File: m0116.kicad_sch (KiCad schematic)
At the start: 247 parts, among them J2 Conn_01x04_MountingPin, J3 Conn_01x04_MountingPin, Q1 Q_PMOS_GSD AO3401A, Q2 Q_NMOS_GSD 2N7002, Q3 Q_NMOS_GSD 2N7002, Q4 2N3904, SW1 SW_Push, U1 XC6206P332MR, U2 74AHCT1G125, U3 STM32F411RETx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

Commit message: updates
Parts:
- removed SW_RGUI_3: mx-alps-nec, Alps_Only:ALPS-1U, symbol MX_Alps_Hybrid:mx-alps-nec
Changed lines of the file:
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@@
     (stroke (width 0) (type default))
   )
-  (wire (pts (xy 186.69 344.17) (xy 186.69 345.44))
-    (stroke (width 0) (type default))
-  )
   (wire (pts (xy 193.04 309.88) (xy 195.58 309.88))
     (stroke (width 0) (type solid))
@@
         )
       )
-    )
-  )
-  (symbol (lib_id "MX_Alps_Hybrid:mx-alps-nec") (at 182.88 346.71 0) (unit 1)
-    (in_bom yes) (on_board yes) (dnp no)
-    (property "Reference" "SW_RGUI_3" (at 183.7182 341.0458 0)
-      (effects (font (size 1.524 1.524)))
-    )
-    (property "Value" "mx-alps-nec" (at 183.7182 342.9254 0)
-      (effects (font (size 0.508 0.508)))
-    )
-    (property "Footprint" "Alps_Only:ALPS-1U" (at 167.005 347.345 0)
-      (effects (font (size 1.524 1.524)) hide)
-    )
-    (property "Datasheet" "" (at 167.005 347.345 0)
-      (effects (font (size 1.524 1.524)) hide)
-    )
-    (pin "1")
-    (pin "2")
-    (instances
-      (project "m0116"
-        (path "/151da08b-0979-4785-a9bf-6fa9b165d629"
-          (reference "SW_RGUI_3") (unit 1)
-        )
-      )

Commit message: fixes
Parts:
- added SW_RALT_4, SW_SP2_4: mx-alps-nec, Alps_Only:ALPS-1U, symbol MX_Alps_Hybrid:mx-alps-nec
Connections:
- net COL6: now also SW_SP2_4.1 (COL)
- net COL8: now also SW_RALT_4.1 (COL)
- net at D7.2 (A), SW_RALT_1.2 (ROW), SW_RALT_2.2 (ROW)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: now also SW_RALT_4.2 (ROW)
- net at D99.2 (A), SW_SP2_1.2 (ROW), SW_SP2_2.2 (ROW)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: now also SW_SP2_4.2 (ROW)
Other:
- note added: "1.25"
- note added: "1.5u"
- note added: "6.25u at101w"
- note added: "6.5u aek"
- note added: "aek"
- note added: "caps 1 is m0116 caps"
- note added: "caps 2 is iso extra rshift for m0118"
- note added: "grid"
- note added: "m0116 with splits"
- note added: "m0118"
- note added: "m0118 iso rsh extra"
- moved on the sheet: D100, D101, D102, D103, D104, D105, D106, D107, D108, D2, D6, D7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

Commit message: fixes
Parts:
- added SW_BACKSL_2: mx-alps-nec, Alps_Only:ALPS-1U, symbol MX_Alps_Hybrid:mx-alps-nec
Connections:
- net COL13: now also SW_BACKSL_2.1 (COL)
- net at D12.2 (A), SW_BACKSL_1.2 (ROW): now also SW_BACKSL_2.2 (ROW)
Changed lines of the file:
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@@
   (junction (at 250.19 285.75) (diameter 0) (color 0 0 0 0)
   )
+  (junction (at 243.84 290.83) (diameter 0) (color 0 0 0 0)
+  )
   (junction (at 233.68 323.85) (diameter 0) (color 0 0 0 0)
   )
@@
     (stroke (width 0) (type default))
   )
+  (wire (pts (xy 243.84 292.1) (xy 243.84 290.83))
+    (stroke (width 0) (type default))
+  )
   (wire (pts (xy 91.44 21.59) (xy 97.79 21.59))
     (stroke (width 0) (type default))
@@
     (stroke (width 0) (type default))
   )
+  (wire (pts (xy 243.84 290.83) (xy 245.11 290.83))
+    (stroke (width 0) (type solid))
+  )
   (wire (pts (xy 233.68 285.75) (xy 233.68 304.8))
     (stroke (width 0) (type solid))
@@
     (stroke (width 0) (type solid))
   )
+  (wire (pts (xy 250.19 285.75) (xy 251.46 285.75))
+    (stroke (width 0) (type default))
+  )
   (wire (pts (xy 36.83 38.1) (xy 36.83 35.56))
     (stroke (width 0) (type default))
@@
     (stroke (width 0) (type default))
   )
+  (wire (pts (xy 251.46 285.75) (xy 251.46 287.02))
+    (stroke (width 0) (type default))
+  )
   (wire (pts (xy 209.55 290.83) (xy 212.09 290.83))
     (stroke (width 0) (type solid))
@@
     (stroke (width 0) (type default))
   )
-  (wire (pts (xy 242.57 290.83) (xy 245.11 290.83))
+  (wire (pts (xy 242.57 290.83) (xy 243.84 290.83))
     (stroke (width 0) (type solid))
   )
@@
     (stroke (width 0) (type solid))
   )
+  (wire (pts (xy 246.38 292.1) (xy 243.84 292.1))
+    (stroke (width 0) (type default))
+  )
   (wire (pts (xy 162.56 361.95) (xy 160.02 361.95))
     (stroke (width 0) (type default))
@@
         )
       )
+    )
+  )
+  (symbol (lib_id "MX_Alps_Hybrid:mx-alps-nec") (at 247.65 288.29 0) (unit 1)
+    (in_bom yes) (on_board yes) (dnp no)
+    (property "Reference" "SW_BACKSL_2" (at 248.4882 282.6258 0)
+      (effects (font (size 1.524 1.524)))
+    )
+    (property "Value" "mx-alps-nec" (at 248.4882 284.5054 0)
+      (effects (font (size 0.508 0.508)))
+    )
+    (property "Footprint" "Alps_Only:ALPS-1U" (at 231.775 288.925 0)
+      (effects (font (size 1.524 1.524)) hide)
+    )
+    (property "Datasheet" "" (at 231.775 288.925 0)
+      (effects (font (size 1.524 1.524)) hide)
+    )
+    (pin "1")
+    (pin "2")
+    (instances
+      (project "m0116"
+        (path "/151da08b-0979-4785-a9bf-6fa9b165d629"
+          (reference "SW_BACKSL_2") (unit 1)
+        )
+      )

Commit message: update
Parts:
- added SW_LALT_4, SW_SP2_5: mx-alps-nec, Alps_Only:ALPS-1U, symbol MX_Alps_Hybrid:mx-alps-nec
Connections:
- net COL3: now also SW_LALT_4.1 (COL)
- net COL6: now also SW_SP2_5.1 (COL)
- net at D99.2 (A), SW_SP2_1.2 (ROW), SW_SP2_2.2 (ROW)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: now also SW_SP2_5.2 (ROW)
- net at D98.2 (A), SW_LALT_1.2 (ROW), SW_LALT_2.2 (ROW)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: now also SW_LALT_4.2 (ROW)
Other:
- note added: "1.5 post-2.5"
- note added: "6.5 post 4"
- moved on the sheet: D98, D99

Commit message: update
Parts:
- added SW_RCTRL_3, SW_RGUI_3: mx-alps-nec, Alps_Only:ALPS-1U, symbol MX_Alps_Hybrid:mx-alps-nec
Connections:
- net COL10: now also SW_RCTRL_3.1 (COL)
- net COL9: now also SW_RGUI_3.1 (COL)
- net at D100.2 (A), SW_RGUI_1.2 (ROW), SW_RGUI_2.2 (ROW): now also SW_RGUI_3.2 (ROW)
- net at D8.2 (A), SW_RCTRL_1.2 (ROW), SW_RCTRL_2.2 (ROW): now also SW_RCTRL_3.2 (ROW)
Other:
- note added: "1.5"
- note added: "1u"
- moved on the sheet: SW_RALT_4
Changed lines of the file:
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@@
   (junction (at 160.02 361.95) (diameter 0) (color 0 0 0 0)
   )
+  (junction (at 160.02 377.19) (diameter 0) (color 0 0 0 0)
+  )
   (junction (at 204.47 65.405) (diameter 0) (color 0 0 0 0)
   )
@@
   (junction (at 196.85 36.83) (diameter 0) (color 0 0 0 0)
   )
+  (junction (at 193.04 377.19) (diameter 0) (color 0 0 0 0)
+  )
   (junction (at 257.81 295.91) (diameter 0) (color 0 0 0 0)
   )
@@
   (junction (at 217.17 285.75) (diameter 1.016) (color 0 0 0 0)
   )
-  (junction (at 160.02 378.46) (diameter 0) (color 0 0 0 0)
-  )
   (junction (at 220.98 29.21) (diameter 0) (color 0 0 0 0)
   )
@@
   (junction (at 233.68 266.7) (diameter 1.016) (color 0 0 0 0)
   )
+  (junction (at 200.66 356.87) (diameter 0) (color 0 0 0 0)
+  )
   (junction (at 298.45 285.75) (diameter 1.016) (color 0 0 0 0)
   )
@@
   (junction (at 127 328.93) (diameter 0) (color 0 0 0 0)
   )
+  (junction (at 176.53 377.19) (diameter 0) (color 0 0 0 0)
+  )
   (junction (at 160.02 396.24) (diameter 0) (color 0 0 0 0)
   )
@@
   (junction (at 167.64 304.8) (diameter 0) (color 0 0 0 0)
   )
+  (junction (at 184.15 356.87) (diameter 0) (color 0 0 0 0)
+  )
   (junction (at 78.74 314.96) (diameter 0) (color 0 0 0 0)
   )
@@
   (junction (at 48.26 334.01) (diameter 0) (color 0 0 0 0)
   )
-  (junction (at 167.64 373.38) (diameter 0) (color 0 0 0 0)
-  )
   (junction (at 265.43 285.75) (diameter 1.016) (color 0 0 0 0)
   )
@@
   (junction (at 208.915 36.83) (diameter 0) (color 0 0 0 0)
   )
+  (junction (at 167.64 372.11) (diameter 0) (color 0 0 0 0)
+  )
   (junction (at 127 334.01) (diameter 1.016) (color 0 0 0 0)
   )
@@
     (stroke (width 0) (type default))
   )
+  (wire (pts (xy 176.53 377.19) (xy 179.07 377.19))
+    (stroke (width 0) (type default))
+  )
   (wire (pts (xy 77.47 118.11) (xy 88.9 118.11))
     (stroke (width 0) (type default))
@@
     (stroke (width 0) (type default))
   )
+  (wire (pts (xy 184.15 356.87) (xy 184.15 372.11))
+    (stroke (width 0) (type default))
+  )
   (wire (pts (xy 110.49 401.32) (xy 110.49 402.59))
     (stroke (width 0) (type default))
@@
     (stroke (width 0) (type default))
   )
-  (wire (pts (xy 160.02 378.46) (xy 160.02 396.24))
-    (stroke (width 0) (type default))
-  )
   (wire (pts (xy 210.82 160.02) (xy 210.82 156.21))
     (stroke (width 0) (type default))
@@
     (stroke (width 0) (type solid))
   )
-  (wire (pts (xy 160.02 378.46) (xy 162.56 378.46))
+  (wire (pts (xy 160.02 377.19) (xy 162.56 377.19))
     (stroke (width 0) (type default))
   )
@@
     (stroke (width 0) (type default))
   )
+  (wire (pts (xy 200.66 356.87) (xy 200.66 372.11))
+    (stroke (width 0) (type default))
+  )
   (wire (pts (xy 106.68 91.44) (xy 125.73 91.44))
     (stroke (width 0) (type default))
@@
     (stroke (width 0) (type default))
   )
+  (wire (pts (xy 193.04 361.95) (xy 193.04 377.19))
+    (stroke (width 0) (type default))
+  )
   (wire (pts (xy 236.22 307.34) (xy 236.22 306.07))
     (stroke (width 0) (type default))
@@
     (stroke (width 0) (type default))
   )
-  (wire (pts (xy 160.02 361.95) (xy 160.02 378.46))
+  (wire (pts (xy 160.02 361.95) (xy 160.02 377.19))
     (stroke (width 0) (type default))
   )
@@
     (stroke (width 0) (type default))
   )
-  (wire (pts (xy 167.64 373.38) (xy 167.64 391.16))
-    (stroke (width 0) (type default))
-  )
   (wire (pts (xy 33.02 347.98) (xy 35.56 347.98))
     (stroke (width 0) (type solid))
@@
     (stroke (width 0) (type default))
   )
-  (wire (pts (xy 167.64 356.87) (xy 167.64 373.38))
+  (wire (pts (xy 167.64 356.87) (xy 167.64 372.11))
     (stroke (width 0) (type default))
   )
@@
     (stroke (width 0) (type default))
   )
-  (wire (pts (xy 193.04 361.95) (xy 193.04 397.51))
-    (stroke (width 0) (type default))
-  )
   (wire (pts (xy 209.55 347.98) (xy 212.09 347.98))
     (stroke (width 0) (type solid))
@@
     (stroke (width 0) (type solid))
   )
+  (wire (pts (xy 160.02 377.19) (xy 160.02 396.24))
+    (stroke (width 0) (type default))
+  )
   (wire (pts (xy 143.51 168.91) (xy 143.51 167.64))
     (stroke (width 0) (type default))
@@
     (stroke (width 0) (type solid))
   )
+  (wire (pts (xy 167.64 372.11) (xy 167.64 391.16))
+    (stroke (width 0) (type default))
+  )
   (wire (pts (xy 143.51 347.98) (xy 143.51 397.51))
     (stroke (width 0) (type default))
@@
     (stroke (width 0) (type default))
   )
-  (wire (pts (xy 176.53 361.95) (xy 176.53 397.51))
+  (wire (pts (xy 176.53 361.95) (xy 176.53 377.19))
     (stroke (width 0) (type default))
   )
@@
     (stroke (width 0) (type solid))
   )
+  (wire (pts (xy 176.53 377.19) (xy 176.53 397.51))
+    (stroke (width 0) (type default))
+  )
   (wire (pts (xy 125.73 378.46) (xy 125.73 397.51))
     (stroke (width 0) (type default))
@@
     (stroke (width 0) (type solid))
   )
+  (wire (pts (xy 193.04 377.19) (xy 195.58 377.19))
+    (stroke (width 0) (type default))
+  )
   (wire (pts (xy 186.69 194.31) (xy 194.31 194.31))
     (stroke (width 0) (type solid))
@@
     (stroke (width 0) (type solid))
   )
+  (wire (pts (xy 193.04 377.19) (xy 193.04 397.51))
+    (stroke (width 0) (type default))
+  )
   (wire (pts (xy 176.53 314.96) (xy 193.04 314.96))
     (stroke (width 0) (type solid))
@@
     (effects (font (size 1.27 1.27)) (justify left bottom))
   )
+  (text "1.5" (at 199.39 375.92 0)
+    (effects (font (size 1.27 1.27)) (justify left bottom))
+  )
   (text "m0118" (at 54.61 375.92 0)
     (effects (font (size 1.27 1.27)) (justify left bottom))
@@
     (effects (font (size 1.27 1.27)) (justify left bottom))
   )
-  (text "1.5u\n" (at 165.1 379.73 0)
+  (text "1u" (at 182.88 377.19 0)
+    (effects (font (size 1.27 1.27)) (justify left bottom))
+  )
+  (text "1.5u\n" (at 165.1 378.46 0)
     (effects (font (size 1.27 1.27)) (justify left bottom))
   )
@@
     )
   )
+  (symbol (lib_id "MX_Alps_Hybrid:mx-alps-nec") (at 196.85 373.38 0) (unit 1)
+    (in_bom yes) (on_board yes) (dnp no)
+    (property "Reference" "SW_RCTRL_3" (at 197.6882 367.7158 0)
+      (effects (font (size 1.524 1.524)))
+    )
+    (property "Value" "mx-alps-nec" (at 197.6882 369.5954 0)
+      (effects (font (size 0.508 0.508)))
+    )
+    (property "Footprint" "Alps_Only:ALPS-1U" (at 180.975 374.015 0)
+      (effects (font (size 1.524 1.524)) hide)
+    )
+    (property "Datasheet" "" (at 180.975 374.015 0)
+      (effects (font (size 1.524 1.524)) hide)
+    )
+    (pin "1")
+    (pin "2")
+    (instances
+      (project "m0116"
+        (path "/151da08b-0979-4785-a9bf-6fa9b165d629"
+          (reference "SW_RCTRL_3") (unit 1)
+        )
+      )
+    )
+  )
   (symbol (lib_id "MX_Alps_Hybrid:mx-alps-nec") (at 294.64 306.07 0) (unit 1)
     (in_bom yes) (on_board yes) (dnp no)
@@
     )
   )
-  (symbol (lib_id "MX_Alps_Hybrid:mx-alps-nec") (at 163.83 374.65 0) (unit 1)
+  (symbol (lib_id "MX_Alps_Hybrid:mx-alps-nec") (at 163.83 373.38 0) (unit 1)
     (in_bom yes) (on_board yes) (dnp no)
-    (property "Reference" "SW_RALT_4" (at 164.6682 368.9858 0)
+    (property "Reference" "SW_RALT_4" (at 164.6682 367.7158 0)
       (effects (font (size 1.524 1.524)))
     )
-    (property "Value" "mx-alps-nec" (at 164.6682 370.8654 0)
+    (property "Value" "mx-alps-nec" (at 164.6682 369.5954 0)
       (effects (font (size 0.508 0.508)))
     )
-    (property "Footprint" "Alps_Only:ALPS-1U" (at 147.955 375.285 0)
+    (property "Footprint" "Alps_Only:ALPS-1U" (at 147.955 374.015 0)
       (effects (font (size 1.524 1.524)) hide)
     )
-    (property "Datasheet" "" (at 147.955 375.285 0)
+    (property "Datasheet" "" (at 147.955 374.015 0)
       (effects (font (size 1.524 1.524)) hide)
     )
@@
         )
       )
+    )
+  )
+  (symbol (lib_id "MX_Alps_Hybrid:mx-alps-nec") (at 180.34 373.38 0) (unit 1)
+    (in_bom yes) (on_board yes) (dnp no)
+    (property "Reference" "SW_RGUI_3" (at 181.1782 367.7158 0)
+      (effects (font (size 1.524 1.524)))
+    )
+    (property "Value" "mx-alps-nec" (at 181.1782 369.5954 0)
+      (effects (font (size 0.508 0.508)))
+    )
+    (property "Footprint" "Alps_Only:ALPS-1U" (at 164.465 374.015 0)
+      (effects (font (size 1.524 1.524)) hide)
+    )
+    (property "Datasheet" "" (at 164.465 374.015 0)
+      (effects (font (size 1.524 1.524)) hide)
+    )
+    (pin "1")
+    (pin "2")
+    (instances
+      (project "m0116"
+        (path "/151da08b-0979-4785-a9bf-6fa9b165d629"
+          (reference "SW_RGUI_3") (unit 1)
+        )
+      )

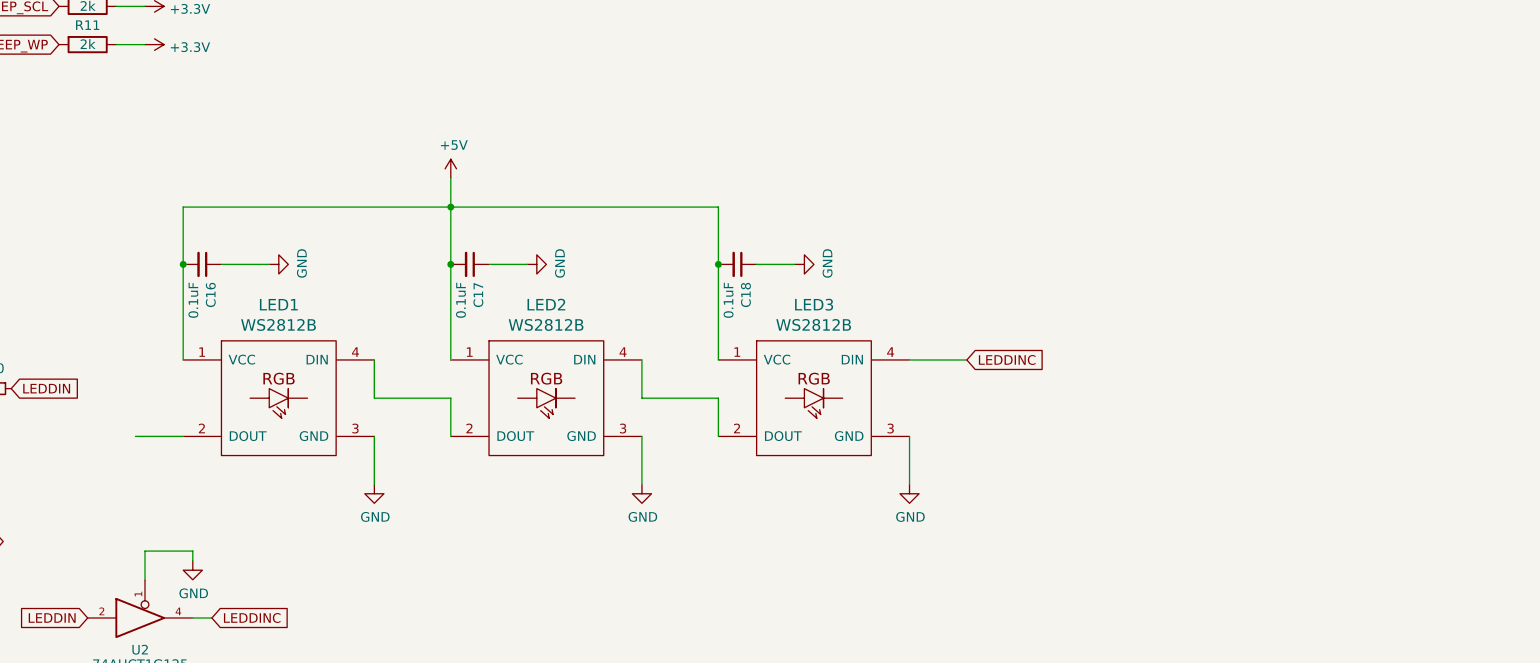
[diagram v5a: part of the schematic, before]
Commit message: add a fourth led
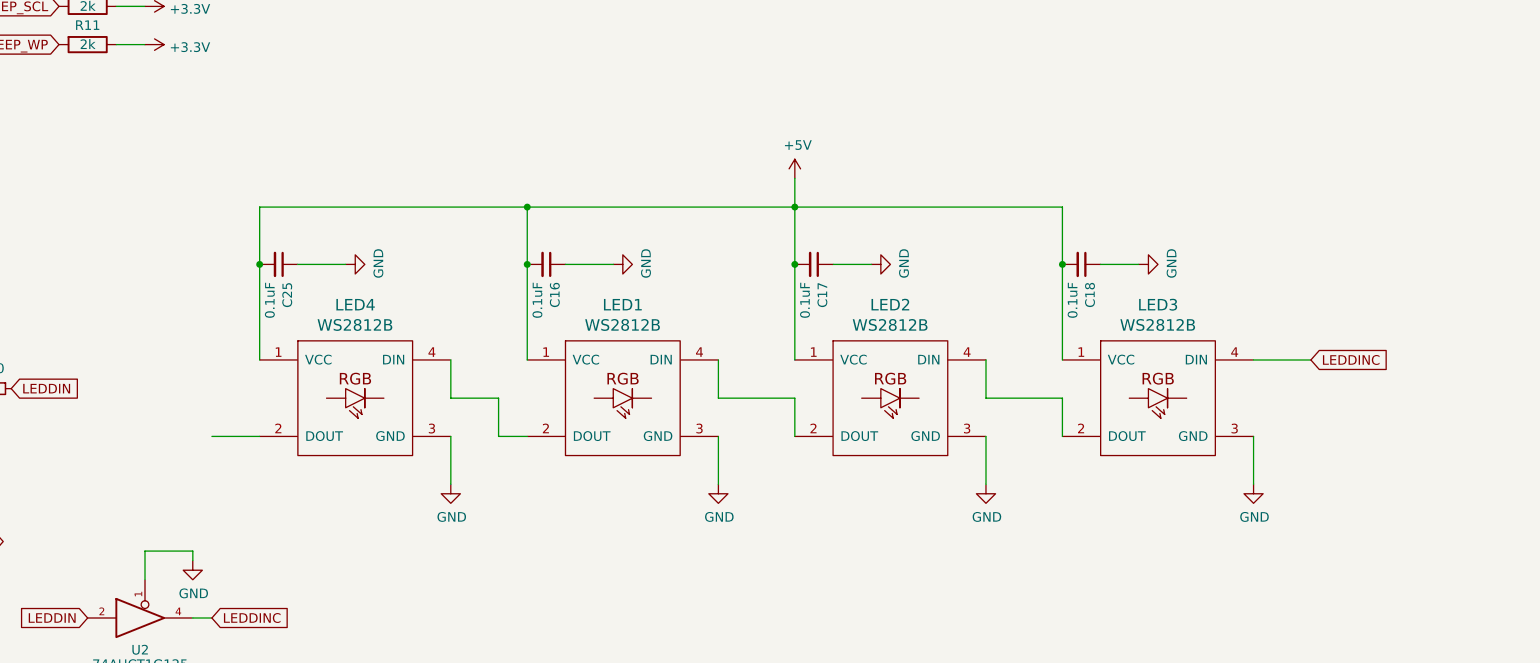
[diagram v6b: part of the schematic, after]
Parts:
- added C25: 0.1uF, Capacitor_SMD:C_0805_2012Metric, symbol Device:C_Small
- added LED4: WS2812B, WS2812B:WS2812BDual, symbol ws2812b:WS2812B
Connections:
- net +5V: now also C25.2, LED4.1 (VCC)
- net GND: now also C25.1, LED4.3 (GND)
- net at LED1.2 (DOUT): now also LED4.4 (DIN)
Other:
- moved on the sheet: C16, C17, C18, LED1, LED2, LED3
